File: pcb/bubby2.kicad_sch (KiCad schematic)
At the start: 7 parts, among them SW1 1825027-8, SW2 1825027-8, SW3 1825027-8, SW4 1825027-8, SW5 1825027-8, SW6 SW_SPST

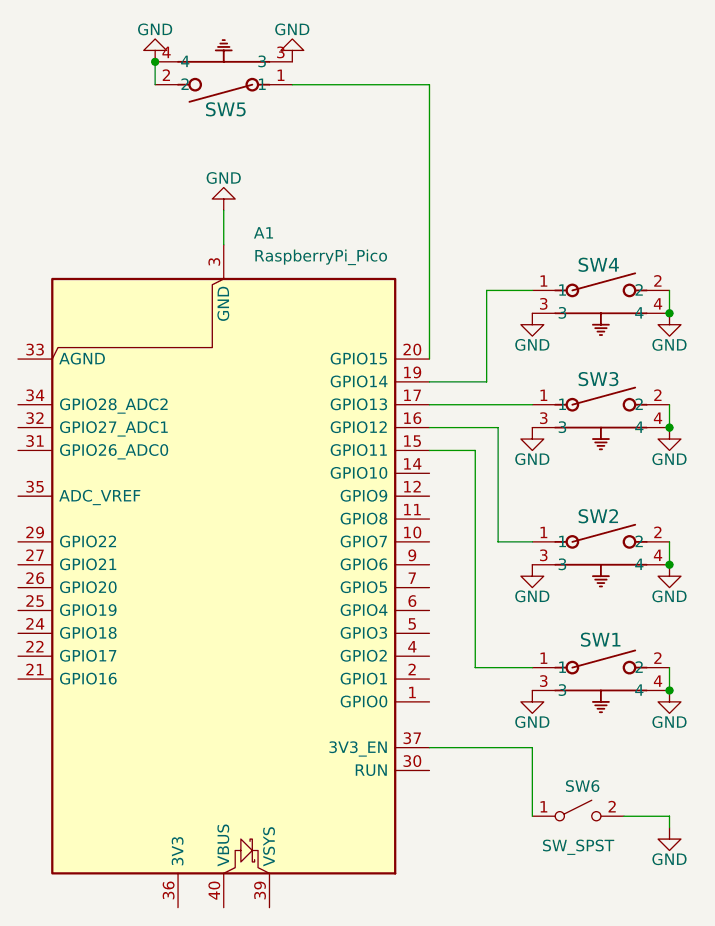
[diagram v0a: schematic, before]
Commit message: pcb routed
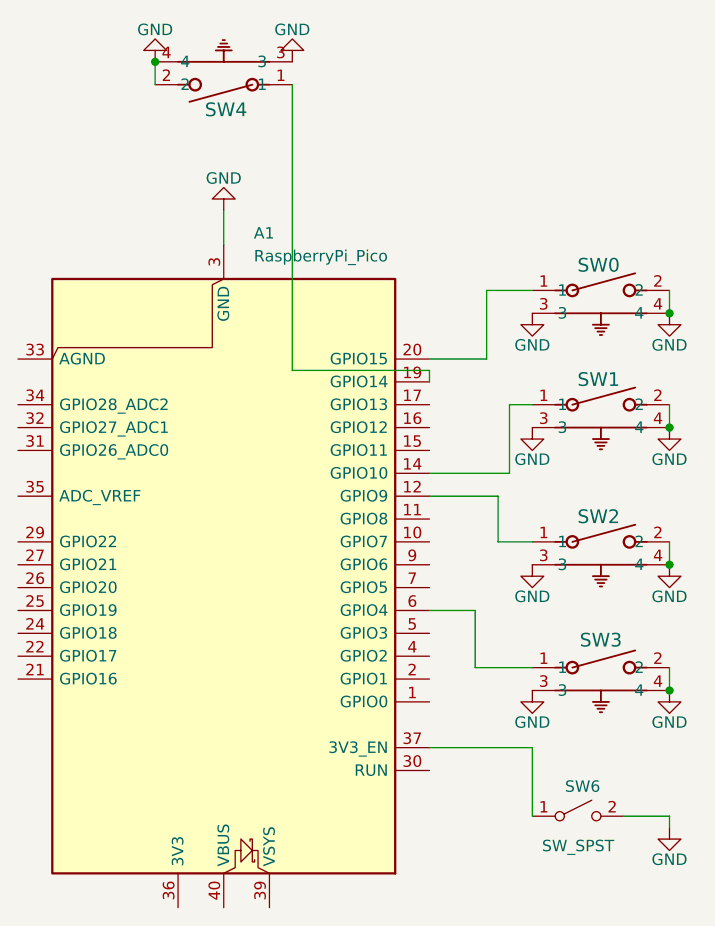
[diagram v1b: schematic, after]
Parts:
- renumbered SW4 to SW0, SW3 to SW1, SW1 to SW3, SW5 to SW4
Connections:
- net at SW3.1: now also A1.6 (GPIO4); no longer A1.15 (GPIO11)
- net at SW4.1: now also A1.19 (GPIO14); no longer A1.20 (GPIO15)
- net at SW0.1: now also A1.20 (GPIO15); no longer A1.19 (GPIO14)
- net at A1.12 (GPIO9): now also SW2.1
- net at A1.14 (GPIO10): now also SW1.1
- net at A1.16 (GPIO12): no longer SW2.1
- net at A1.17 (GPIO13): no longer SW1.1
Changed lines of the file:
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@@
+	(wire
+		(pts
+			(xy 248.92 101.6) (xy 241.3 101.6)
+		)
+		(stroke
+			(width 0)
+			(type default)
+		)
+	)
+	(wire
+		(pts
+			(xy 241.3 87.63) (xy 241.3 88.9)
+		)
+		(stroke
+			(width 0)
+			(type default)
+		)
+	)
 	(wire
 		(pts
@@
 	(wire
 		(pts
-			(xy 241.3 93.98) (xy 248.92 93.98)
-		)
-		(stroke
-			(width 0)
-			(type default)
-		)
-	)
-	(wire
-		(pts
-			(xy 241.3 96.52) (xy 246.38 96.52)
-		)
-		(stroke
-			(width 0)
-			(type default)
-		)
-	)
-	(wire
-		(pts
 			(xy 241.3 129.54) (xy 252.73 129.54)
 		)
@@
 	(wire
 		(pts
-			(xy 247.65 88.9) (xy 247.65 78.74)
-		)
-		(stroke
-			(width 0)
-			(type default)
-		)
-	)
-	(wire
-		(pts
-			(xy 246.38 96.52) (xy 246.38 120.65)
+			(xy 250.19 91.44) (xy 252.73 91.44)
+		)
+		(stroke
+			(width 0)
+			(type default)
+		)
+	)
+	(wire
+		(pts
+			(xy 226.06 87.63) (xy 241.3 87.63)
+		)
+		(stroke
+			(width 0)
+			(type default)
+		)
+	)
+	(wire
+		(pts
+			(xy 241.3 86.36) (xy 247.65 86.36)
+		)
+		(stroke
+			(width 0)
+			(type default)
+		)
+	)
+	(wire
+		(pts
+			(xy 250.19 99.06) (xy 250.19 91.44)
 		)
 		(stroke
@@
 	(wire
 		(pts
-			(xy 241.3 88.9) (xy 247.65 88.9)
-		)
-		(stroke
-			(width 0)
-			(type default)
-		)
-	)
-	(wire
-		(pts
-			(xy 241.3 91.44) (xy 252.73 91.44)
-		)
-		(stroke
-			(width 0)
-			(type default)
-		)
-	)
-	(wire
-		(pts
-			(xy 241.3 55.88) (xy 226.06 55.88)
-		)
-		(stroke
-			(width 0)
-			(type default)
-		)
-	)
-	(wire
-		(pts
-			(xy 248.92 93.98) (xy 248.92 106.68)
+			(xy 241.3 99.06) (xy 250.19 99.06)
+		)
+		(stroke
+			(width 0)
+			(type default)
+		)
+	)
+	(wire
+		(pts
+			(xy 248.92 106.68) (xy 248.92 101.6)
+		)
+		(stroke
+			(width 0)
+			(type default)
+		)
+	)
+	(wire
+		(pts
+			(xy 226.06 55.88) (xy 226.06 87.63)
+		)
+		(stroke
+			(width 0)
+			(type default)
+		)
+	)
+	(wire
+		(pts
+			(xy 241.3 114.3) (xy 246.38 114.3)
+		)
+		(stroke
+			(width 0)
+			(type default)
+		)
+	)
+	(wire
+		(pts
+			(xy 247.65 86.36) (xy 247.65 78.74)
 		)
 		(stroke
@@
 	(wire
 		(pts
+			(xy 246.38 114.3) (xy 246.38 120.65)
+		)
+		(stroke
+			(width 0)
+			(type default)
+		)
+	)
+	(wire
+		(pts
 			(xy 246.38 120.65) (xy 252.73 120.65)
-		)
-		(stroke
-			(width 0)
-			(type default)
-		)
-	)
-	(wire
-		(pts
-			(xy 241.3 86.36) (xy 241.3 55.88)
 		)
 		(stroke
@@
 		(on_board yes)
 		(dnp no)
-		(property "Reference" "SW1"
+		(property "Reference" "SW3"
 			(at 260.35 117.602 0)
 			(effects
@@
 			(project "bubby2"
 				(path "/d86e1757-a987-4b54-ba96-718471fe940c"
-					(reference "SW1")
+					(reference "SW3")
 					(unit 1)
 				)
@@
 		(on_board yes)
 		(dnp no)
-		(property "Reference" "SW5"
+		(property "Reference" "SW4"
 			(at 218.694 58.674 0)
 			(effects
@@
 			(project "bubby2"
 				(path "/d86e1757-a987-4b54-ba96-718471fe940c"
-					(reference "SW5")
+					(reference "SW4")
 					(unit 1)
 				)
@@
 		(on_board yes)
 		(dnp no)
-		(property "Reference" "SW4"
+		(property "Reference" "SW0"
 			(at 260.096 75.946 0)
 			(effects
@@
 			(project "bubby2"
 				(path "/d86e1757-a987-4b54-ba96-718471fe940c"
-					(reference "SW4")
+					(reference "SW0")
 					(unit 1)
 				)
@@
 		(on_board yes)
 		(dnp no)
-		(property "Reference" "SW3"
+		(property "Reference" "SW1"
 			(at 260.096 88.646 0)
 			(effects
@@
 			(project "bubby2"
 				(path "/d86e1757-a987-4b54-ba96-718471fe940c"
-					(reference "SW3")
-					(unit 1)
-				)
+					(reference "SW1")
+					(unit 1)
+				)

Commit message: no DRC errors!
changed schematic parts to remove all DRC issues.
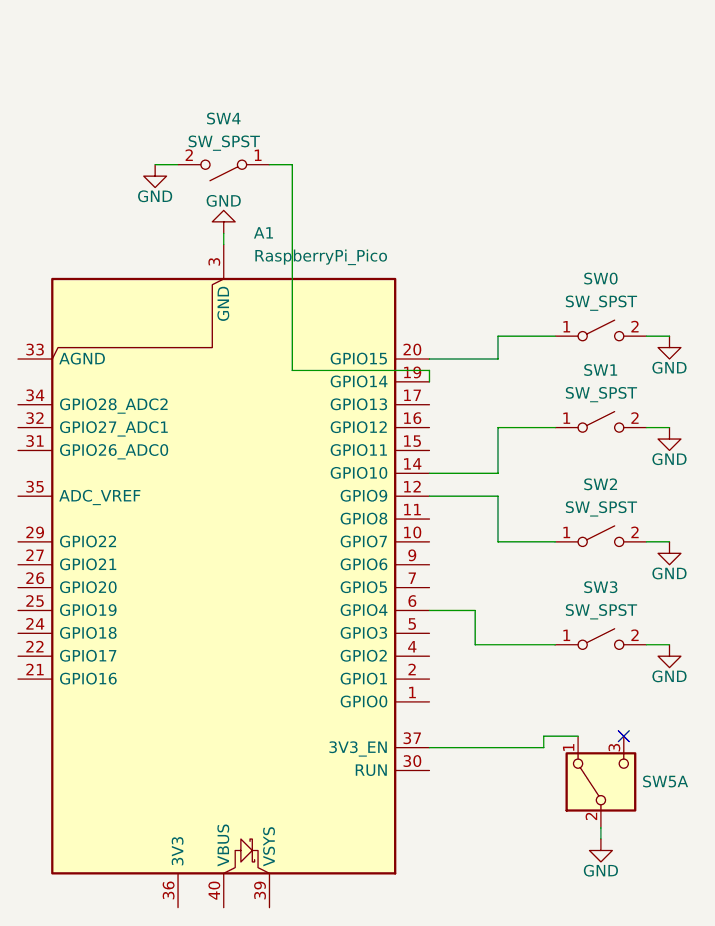
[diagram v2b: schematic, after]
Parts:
- removed SW0, SW1, SW2, SW3, SW4: 1825027-8, Button_Switch_SMD:Panasonic_EVQPUL_EVQPUC, symbol 2024-07-22_18-52-54:1825027-8
- removed SW6: SW_SPST, footprints:sw_spdt_slide_mskt-12c03, symbol Switch:SW_SPST
- added SW0, SW1, SW2, SW3, SW4: SW_SPST, Button_Switch_SMD:Panasonic_EVQPUL_EVQPUC, symbol sw_spst_rt_ang_tactile:SW_SPST
- added SW5: SW_DPDT_x2, footprints:sw_spdt_slide_mskt-12c03, symbol Switch:SW_DPDT_x2
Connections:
- net GND: now also SW0.2 (B), SW1.2 (B), SW2.2 (B), SW3.2 (B), SW4.2 (B), SW5.2 (B)
- net at A1.6 (GPIO4): now also SW3.1 (A)
- net at A1.19 (GPIO14): now also SW4.1 (A)
- net at A1.37 (3V3_EN): now also SW5.1 (A)
- net at A1.20 (GPIO15): now also SW0.1 (A)
- net at A1.12 (GPIO9): now also SW2.1 (A)
- net at A1.14 (GPIO10): now also SW1.1 (A)
- no-connect marks 0 -> 1

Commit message: minor fit changes
moved a button, added a screw hole...
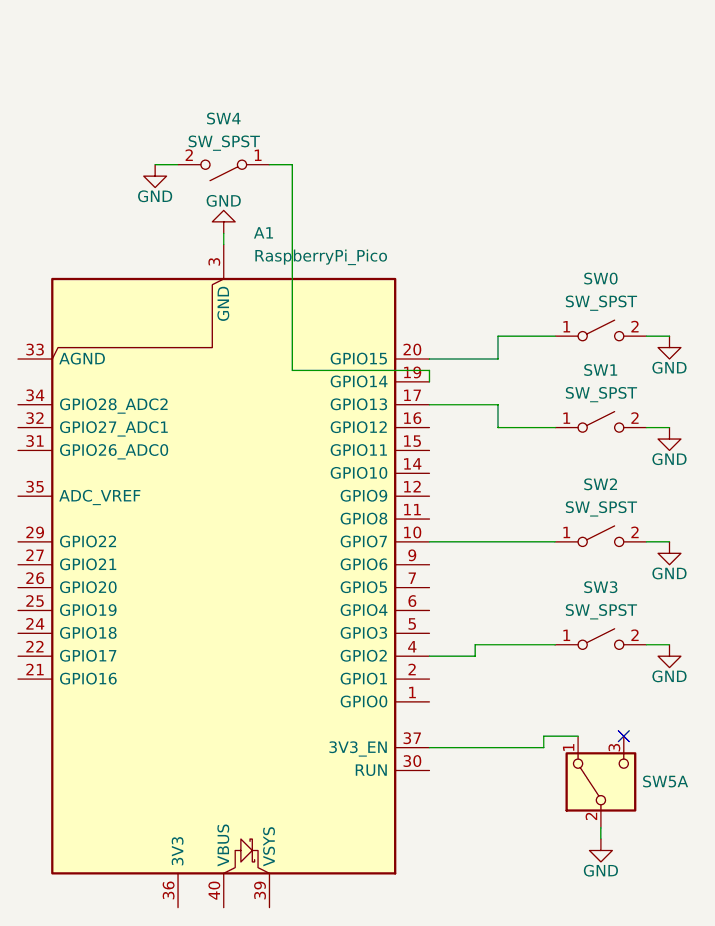
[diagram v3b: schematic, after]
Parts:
- SW5: footprint footprints:sw_spdt_slide_mskt-12c03 -> sw_spdt_slide_mskt-12c03:Untitled
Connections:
- net at SW1.1 (A): now also A1.17 (GPIO13); no longer A1.14 (GPIO10)
- net at A1.10 (GPIO7): now also SW2.1 (A)
- net at A1.12 (GPIO9): no longer SW2.1 (A)
- net at A1.4 (GPIO2): now also SW3.1 (A)
- net at A1.6 (GPIO4): no longer SW3.1 (A)
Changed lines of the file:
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@@
-	(wire
-		(pts
-			(xy 248.92 106.68) (xy 255.27 106.68)
-		)
-		(stroke
-			(width 0)
-			(type default)
-		)
-	)
-	(wire
-		(pts
-			(xy 248.92 101.6) (xy 241.3 101.6)
-		)
-		(stroke
-			(width 0)
-			(type default)
-		)
-	)
 	(wire
 		(pts
@@
 	(wire
 		(pts
+			(xy 241.3 106.68) (xy 255.27 106.68)
+		)
+		(stroke
+			(width 0)
+			(type default)
+		)
+	)
+	(wire
+		(pts
 			(xy 223.52 64.77) (xy 226.06 64.77)
 		)
@@
 	(wire
 		(pts
+			(xy 246.38 119.38) (xy 246.38 118.11)
+		)
+		(stroke
+			(width 0)
+			(type default)
+		)
+	)
+	(wire
+		(pts
 			(xy 218.44 72.39) (xy 218.44 73.66)
 		)
@@
 	(wire
 		(pts
-			(xy 248.92 93.98) (xy 248.92 99.06)
+			(xy 241.3 91.44) (xy 248.92 91.44)
 		)
 		(stroke
@@
 	(wire
 		(pts
-			(xy 241.3 99.06) (xy 248.92 99.06)
-		)
-		(stroke
-			(width 0)
-			(type default)
-		)
-	)
-	(wire
-		(pts
-			(xy 248.92 106.68) (xy 248.92 101.6)
-		)
-		(stroke
-			(width 0)
-			(type default)
-		)
-	)
-	(wire
-		(pts
-			(xy 241.3 114.3) (xy 246.38 114.3)
+			(xy 241.3 119.38) (xy 246.38 119.38)
 		)
 		(stroke
@@
 	(wire
 		(pts
+			(xy 248.92 91.44) (xy 248.92 93.98)
+		)
+		(stroke
+			(width 0)
+			(type default)
+		)
+	)
+	(wire
+		(pts
 			(xy 248.92 86.36) (xy 248.92 83.82)
 		)
@@
 		(pts
 			(xy 254 129.54) (xy 241.3 129.54)
-		)
-		(stroke
-			(width 0)
-			(type default)
-		)
-	)
-	(wire
-		(pts
-			(xy 246.38 114.3) (xy 246.38 118.11)
 		)
 		(stroke
@@
 			)
 		)
-		(property "Footprint" "footprints:sw_spdt_slide_mskt-12c03"
+		(property "Footprint" "sw_spdt_slide_mskt-12c03:Untitled"
 			(at 260.35 133.35 0)
 			(effects
